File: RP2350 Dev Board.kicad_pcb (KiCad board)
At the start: 4 copper layers, 84.8 x 23.7 mm, 60 parts, among them J1 Conn_01x32_MountingPin, J2 Conn_01x03_Pin, J3 Conn_01x32_MountingPin, U4 Winbond W25Q128JVSIQ, U5 RPI Radio Module 2, U6 ESP-PSRAM32

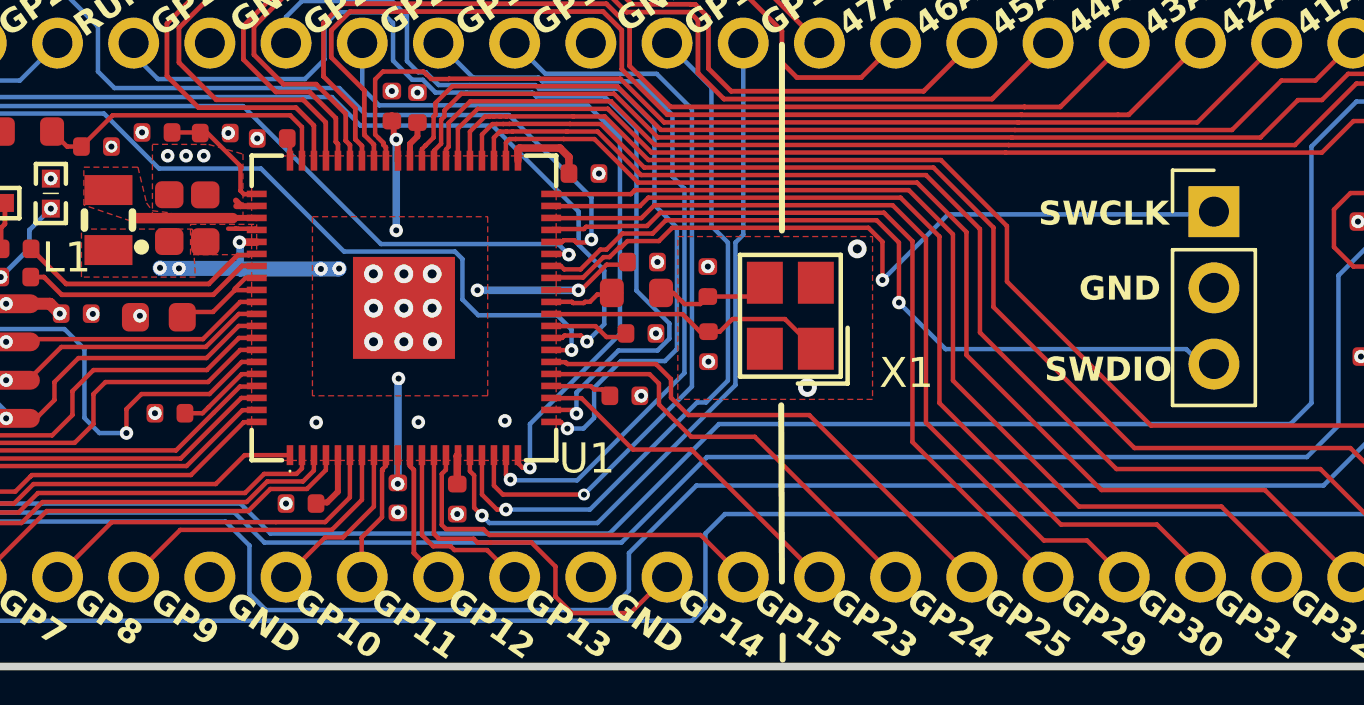
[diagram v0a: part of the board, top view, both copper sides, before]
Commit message: Cleanup of connectors
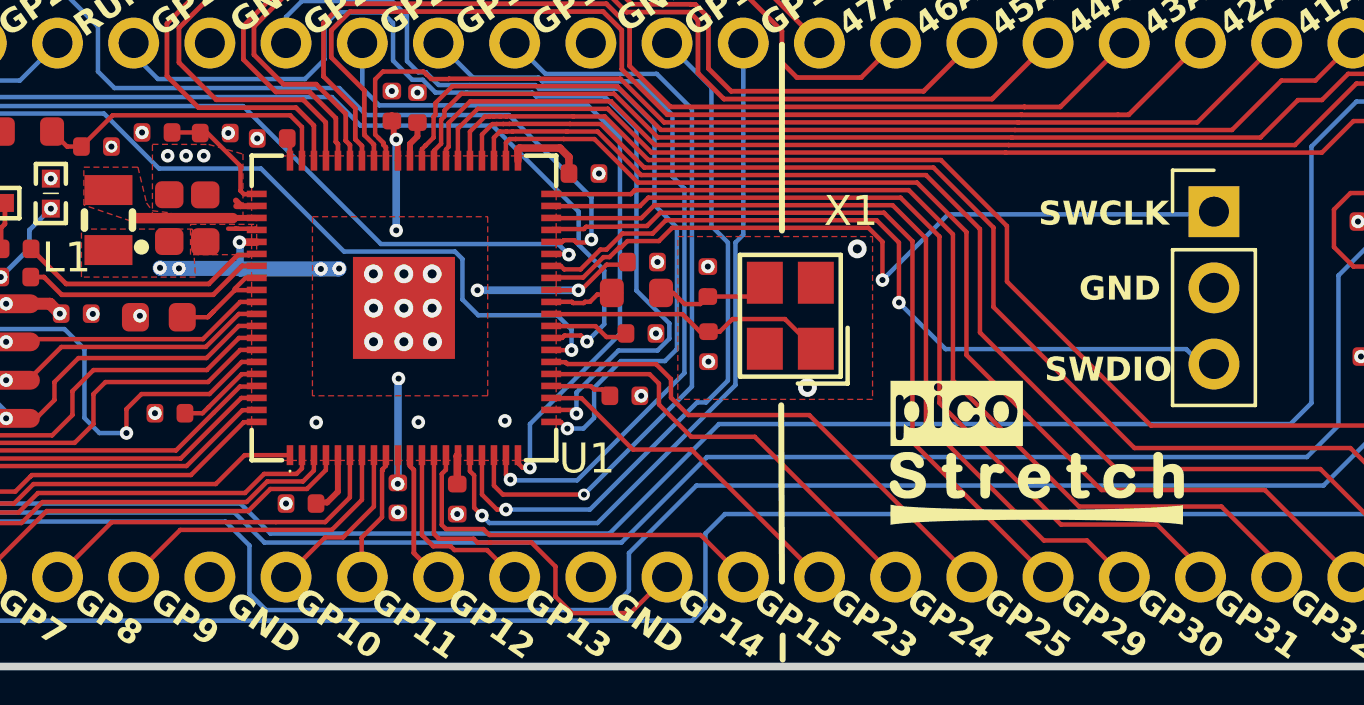
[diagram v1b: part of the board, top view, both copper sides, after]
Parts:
- added G***: LOGO, Custom:logo, F.Cu at (167.5, 107.2)
- added G***: LOGO, Custom:logo_large, B.Cu at (160.7, 103.0)
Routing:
- net 3V3: track 24.0 -> 24.7 mm

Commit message: Before RM2 reset
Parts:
- added TP1: TestPoint, TestPoint:TestPoint_Pad_1.0x1.0mm, B.Cu at (145.4, 102.2)
- added TP2: TestPoint, TestPoint:TestPoint_Pad_1.0x1.0mm, B.Cu at (123.5, 100.8)
- moved PWR_LED1 12.4 mm to (124.7, 105.5), turned to 0 degrees
- moved JP1 0.40 mm to (111.6, 107.8)
- moved JP3 0.40 mm to (115.4, 107.8)
- moved JP2 0.30 mm to (124.2, 107.8)
- moved R12 0.25 mm to (120.8, 105.6), turned to 180 degrees
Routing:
- net Net-(PWR_LED1-Pad1): track 7.67 -> 2.60 mm
- net 3V3: track 24.7 -> 25.7 mm, vias 14 -> 13
- net 1V1: track 23.1 -> 23.8 mm, vias 11 -> 12
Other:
- board text added: "1v1"
- board text added: "3v3"

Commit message: Cleanup
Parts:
- moved JP3 48.0 mm to (163.3, 106.8)
- moved JP2 45.5 mm to (169.7, 106.7)
- turned C16 to 0 degrees
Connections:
- C16 pad 1: GND -> 3V3
- C16 pad 2: 3V3 -> GND
- JP2 pad 2: GPIO4 -> GPIO25
- JP3 pad 1: GPIO1 -> GPIO23
- R15 pad 2: GPIO3 -> GPIO24
- R16 pad 1: GPIO3 -> GPIO24
- U5 pad 3: GPIO2 -> GPIO29
- U5 pad 5: GPIO3 -> GPIO24
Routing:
- net GPIO2: track 112.5 -> 26.7 mm, vias 1 -> 0
- net GPIO3: track 107.3 -> 24.0 mm, vias 3 -> 0
- net Net-(JP3-B): track 83.2 -> 24.7 mm
- net GPIO24: track 14.7 -> 60.6 mm, vias 0 -> 3
- net Net-(JP2-A): track 66.2 -> 27.4 mm, vias 1 -> 2
- net GPIO29: track 25.7 -> 62.5 mm, vias 0 -> 1
- net GPIO25: track 17.3 -> 22.8 mm
- net GPIO23: track 11.4 -> 15.5 mm
- net GPIO1: track 34.7 -> 32.0 mm
- net GPIO4: track 24.6 -> 22.3 mm
